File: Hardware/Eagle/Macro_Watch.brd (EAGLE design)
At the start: 26.7 x 38.4 mm, 40 parts, among them M1 MF-LED-0603-RED, M16 MF-LED-0603-RED, M2 MF-LED-0603-RED, M32 MF-LED-0603-RED, M4 MF-LED-0603-RED, M8 MF-LED-0603-RED, U1 EFM8SB10F2G-A-QFN20R, X1 ECS-.327-12.5-34B-TR

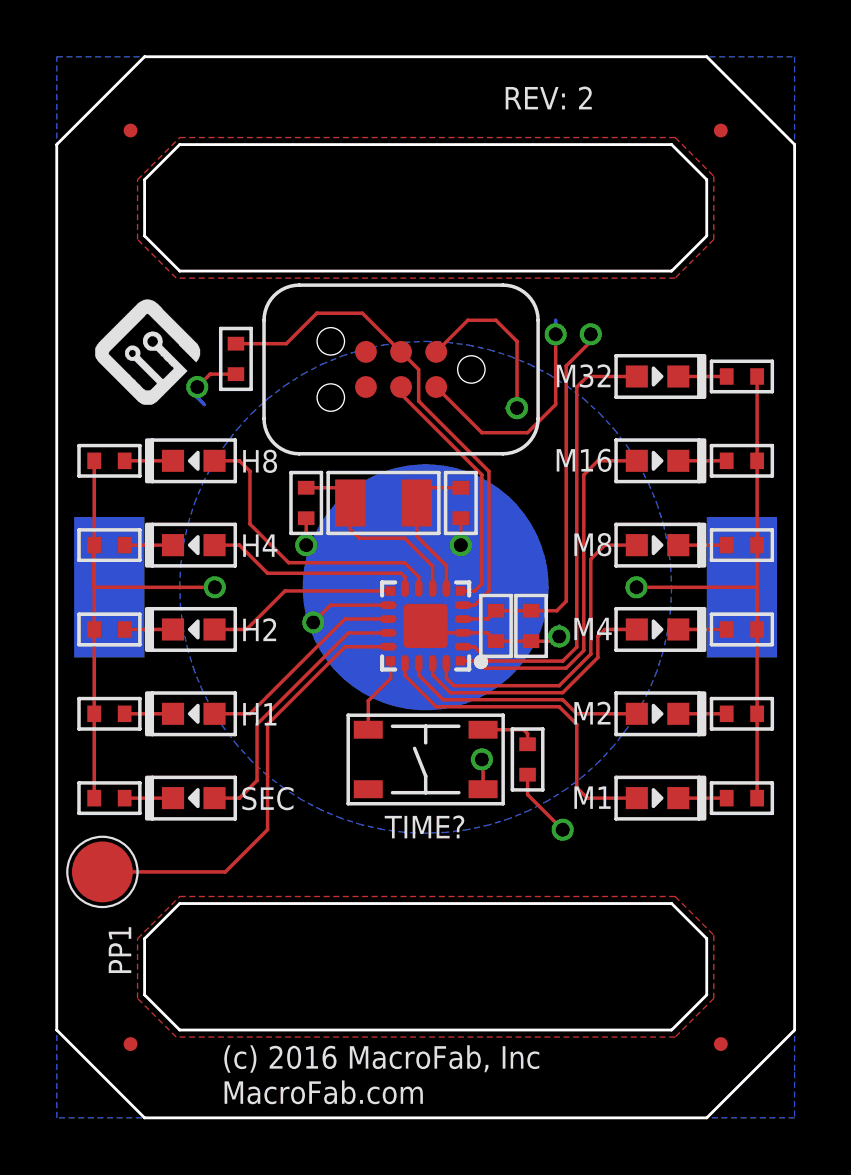
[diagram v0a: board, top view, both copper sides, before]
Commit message: Updated files to latest Library.
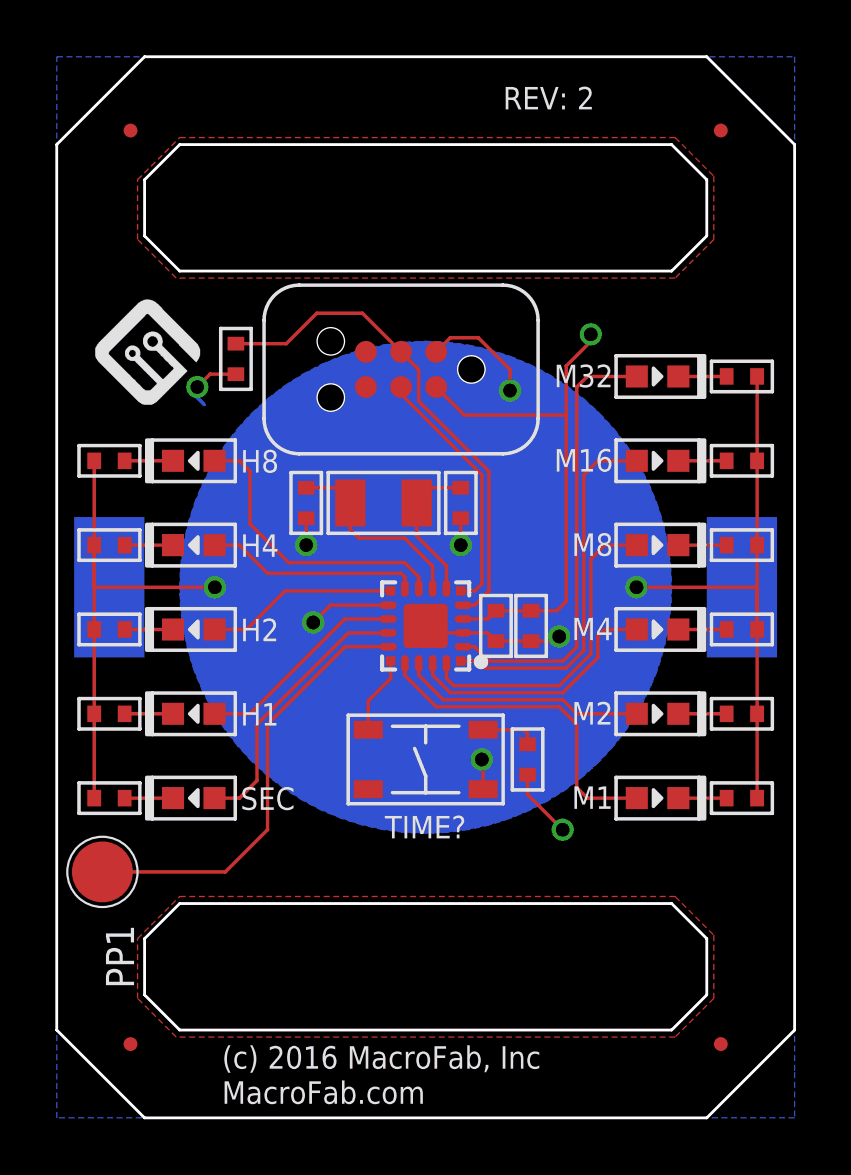
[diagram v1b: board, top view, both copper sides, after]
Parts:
- removed J1: (no value), PP_Connectors:TC2030
- added TC1: TC2030-IDC-NL, MF_Connectors:TC2030-IDC-NL
- C1: value MF-CAP-0402-1uF -> 1uF
- C2: value MF-CAP-0402-0.1uF -> 0.1uF
- C4, C5: value 500R07S120KV4T -> 12pF
- FID1, FID2, FID3, FID4: value FIDUCIAL_0.5MM -> (none)
- FRAME1: value MF_FRAMEDEFAULT -> (none)
- R1, R2: value MF-RES-0402-10K -> 10K
- R10, R11, R12, R13, R3, R4, R5, R6, R7, R8, R9: value MF-RES-0402-75 -> 75
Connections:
- net 3.0V: now also TC1.P$2; no longer J1.P$2
- net C2CK: now also TC1.P$3; no longer J1.P$3
- net C2D: now also TC1.P$4; no longer J1.P$4
- net GND: now also TC1.P$1; no longer J1.P$1
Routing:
- net 3.0V: track 27.7 -> 24.4 mm, vias 4 -> 3
- net GND: track 58.8 -> 56.8 mm
